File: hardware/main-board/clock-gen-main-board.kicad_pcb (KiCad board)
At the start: 2 copper layers, 70 x 50 mm, 18 parts, among them J1 Conn_01x03_Pin, J2 Conn_01x03_Pin, J3 Conn_01x02_Pin, J4 Conn_01x01_Pin, J5 Conn_01x01_Pin, J6 Conn_01x01_Pin, J7 Conn_01x01_Pin, U1 Pico

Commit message: fix iovdd
- create new gerbers
- create new render
- update readme
- update changelog
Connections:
- U1 pad 36: /PCM.3V3 -> /Gen.VSI
- U1 pad 39: /Gen.VSI -> unconnected-(U1-VSYS-Pad39)
- U3 pad 2: /PCM.3V3 -> /Gen.VSI
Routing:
- net /PCM.3V3: track 62.1 -> 0.00 mm
- net /Gen.VSI: track 50.9 -> 109.0 mm
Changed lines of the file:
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@@
   (title_block
     (title "${proj-title}")
-    (date "2023-09-16")
+    (date "2023-09-23")
     (rev "${proj-version}")
     (company "${proj-author}")
@@
   (property "proj-license" "CC BY-SA 4.0")
   (property "proj-title" "clock-gen adc main board")
-  (property "proj-version" "A")
+  (property "proj-version" "B")
   (net 0 "")
   (net 1 "unconnected-(U1-GPIO0-Pad1)")
@@
   (net 14 "unconnected-(U1-GPIO15-Pad20)")
   (net 15 "Net-(D1-K)")
-  (net 16 "/PCM.3V3")
+  (net 16 "unconnected-(U1-VSYS-Pad39)")
   (net 17 "/PCM.Data")
   (net 18 "/PCM.BitClk")
@@
       (net 33 "/PCM.5V") (pinfunction "+5V") (pintype "power_in"))
     (pad "2" thru_hole circle (at -7.62 -2 180) (size 2 2) (drill 1.25) (layers "*.Cu" "*.Mask")
-      (net 16 "/PCM.3V3") (pinfunction "+3.3V") (pintype "power_in"))
+      (net 38 "/Gen.VSI") (pinfunction "+3.3V") (pintype "power_in"))
     (pad "3" thru_hole circle (at -5.08 -2 180) (size 2 2) (drill 1.25) (layers "*.Cu" "*.Mask")
       (net 30 "GND") (pinfunction "GND") (pintype "power_in"))
@@
       (net 25 "unconnected-(U1-ADC_VREF-Pad35)") (pinfunction "ADC_VREF") (pintype "power_in+no_connect"))
     (pad "36" thru_hole oval (at 8.89 -13.97 90) (size 1.7 1.7) (drill 1.02) (layers "*.Cu" "*.Mask")
-      (net 16 "/PCM.3V3") (pinfunction "3V3") (pintype "power_in"))
+      (net 38 "/Gen.VSI") (pinfunction "3V3") (pintype "power_in"))
     (pad "36" smd rect (at 8.89 -13.97 90) (size 3.5 1.7) (drill (offset 0.9 0)) (layers "F.Cu" "F.Mask")
-      (net 16 "/PCM.3V3") (pinfunction "3V3") (pintype "power_in"))
+      (net 38 "/Gen.VSI") (pinfunction "3V3") (pintype "power_in"))
     (pad "37" thru_hole oval (at 8.89 -16.51 90) (size 1.7 1.7) (drill 1.02) (layers "*.Cu" "*.Mask")
       (net 26 "unconnected-(U1-3V3_EN-Pad37)") (pinfunction "3V3_EN") (pintype "input+no_connect"))
@@
       (net 30 "GND") (pinfunction "GND") (pintype "bidirectional"))
     (pad "39" thru_hole oval (at 8.89 -21.59 90) (size 1.7 1.7) (drill 1.02) (layers "*.Cu" "*.Mask")
-      (net 38 "/Gen.VSI") (pinfunction "VSYS") (pintype "power_in"))
+      (net 16 "unconnected-(U1-VSYS-Pad39)") (pinfunction "VSYS") (pintype "power_in+no_connect"))
     (pad "39" smd rect (at 8.89 -21.59 90) (size 3.5 1.7) (drill (offset 0.9 0)) (layers "F.Cu" "F.Mask")
-      (net 38 "/Gen.VSI") (pinfunction "VSYS") (pintype "power_in"))
+      (net 16 "unconnected-(U1-VSYS-Pad39)") (pinfunction "VSYS") (pintype "power_in+no_connect"))
     (pad "40" thru_hole oval (at 8.89 -24.13 90) (size 1.7 1.7) (drill 1.02) (layers "*.Cu" "*.Mask")
       (net 33 "/PCM.5V") (pinfunction "VBUS") (pintype "power_in"))
@@
   (segment (start 148.63 91.16) (end 148.63 87.83) (width 0.25) (layer "F.Cu") (net 15))
   (segment (start 148.63 87.83) (end 145.55 84.75) (width 0.25) (layer "F.Cu") (net 15))
-  (segment (start 152.2 105.6) (end 156.37 109.77) (width 0.25) (layer "F.Cu") (net 16))
-  (segment (start 156.37 109.77) (end 156.37 116.4345) (width 0.25) (layer "F.Cu") (net 16))
-  (segment (start 111 94.8) (end 119.2 94.8) (width 0.25) (layer "F.Cu") (net 16))
-  (segment (start 119.2 94.8) (end 130 105.6) (width 0.25) (layer "F.Cu") (net 16))
-  (segment (start 110.6 91.23) (end 110.6 94.4) (width 0.25) (layer "F.Cu") (net 16))
-  (segment (start 110.6 94.4) (end 111 94.8) (width 0.25) (layer "F.Cu") (net 16))
-  (segment (start 110.53 91.16) (end 110.6 91.23) (width 0.25) (layer "F.Cu") (net 16))
-  (segment (start 130 105.6) (end 152.2 105.6) (width 0.25) (layer "F.Cu") (net 16))
   (segment (start 150.4 104.6) (end 152 106.2) (width 0.25) (layer "B.Cu") (net 17))
   (segment (start 152 106.2) (end 152 114) (width 0.25) (layer "B.Cu") (net 17))
@@
   (segment (start 141.4 118.8) (end 141.13 118.53) (width 0.25) (layer "F.Cu") (net 37))
   (segment (start 160.2 118.8) (end 141.4 118.8) (width 0.25) (layer "F.Cu") (net 37))
-  (segment (start 102.91 92.91) (end 107.6 97.6) (width 0.25) (layer "F.Cu") (net 38))
   (segment (start 99 106.6) (end 99 114) (width 0.25) (layer "F.Cu") (net 38))
+  (segment (start 152.2 105.6) (end 156.37 109.77) (width 0.25) (layer "F.Cu") (net 38))
+  (segment (start 156.37 109.77) (end 156.37 116.4345) (width 0.25) (layer "F.Cu") (net 38))
   (segment (start 99 114) (end 99.4 114.4) (width 0.25) (layer "F.Cu") (net 38))
+  (segment (start 111 94.8) (end 119.2 94.8) (width 0.25) (layer "F.Cu") (net 38))
   (segment (start 101.6 114.4) (end 113.244 126.044) (width 0.25) (layer "F.Cu") (net 38))
   (segment (start 107.6 103.4) (end 104.8 106.2) (width 0.25) (layer "F.Cu") (net 38))
   (segment (start 113.244 126.044) (end 113.38 126.044) (width 0.25) (layer "F.Cu") (net 38))
+  (segment (start 119.2 94.8) (end 130 105.6) (width 0.25) (layer "F.Cu") (net 38))
+  (segment (start 110.6 91.23) (end 110.6 94.4) (width 0.25) (layer "F.Cu") (net 38))
   (segment (start 99.4 114.4) (end 101.6 114.4) (width 0.25) (layer "F.Cu") (net 38))
-  (segment (start 102.91 91.16) (end 102.91 92.91) (width 0.25) (layer "F.Cu") (net 38))
+  (segment (start 110.6 94.6) (end 110.6 94.4) (width 0.25) (layer "F.Cu") (net 38))
+  (segment (start 110.6 94.4) (end 111 94.8) (width 0.25) (layer "F.Cu") (net 38))
   (segment (start 99.4 106.2) (end 99 106.6) (width 0.25) (layer "F.Cu") (net 38))
+  (segment (start 110.53 91.16) (end 110.6 91.23) (width 0.25) (layer "F.Cu") (net 38))
   (segment (start 107.6 97.6) (end 107.6 103.4) (width 0.25) (layer "F.Cu") (net 38))
+  (segment (start 107.6 97.6) (end 110.6 94.6) (width 0.25) (layer "F.Cu") (net 38))
   (segment (start 104.8 106.2) (end 99.4 106.2) (width 0.25) (layer "F.Cu") (net 38))
+  (segment (start 130 105.6) (end 152.2 105.6) (width 0.25) (layer "F.Cu") (net 38))
   (segment (start 130.6 83.8) (end 126.25 83.8) (width 0.25) (layer "F.Cu") (net 40))
   (segment (start 135 83.8) (end 130.6 83.8) (width 0.25) (layer "F.Cu") (net 40))

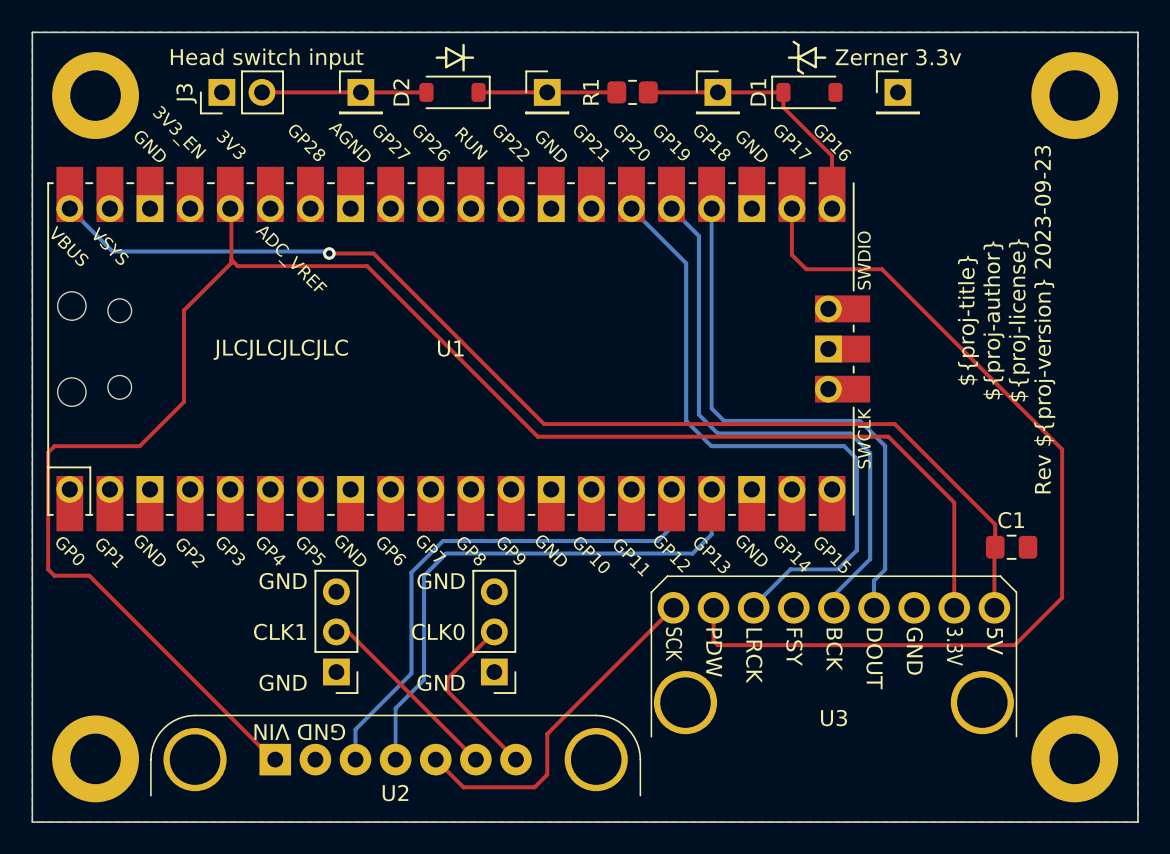
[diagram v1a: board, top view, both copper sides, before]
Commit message: Resolve "PCM1802 board 3.3V pin is driven instead of open"
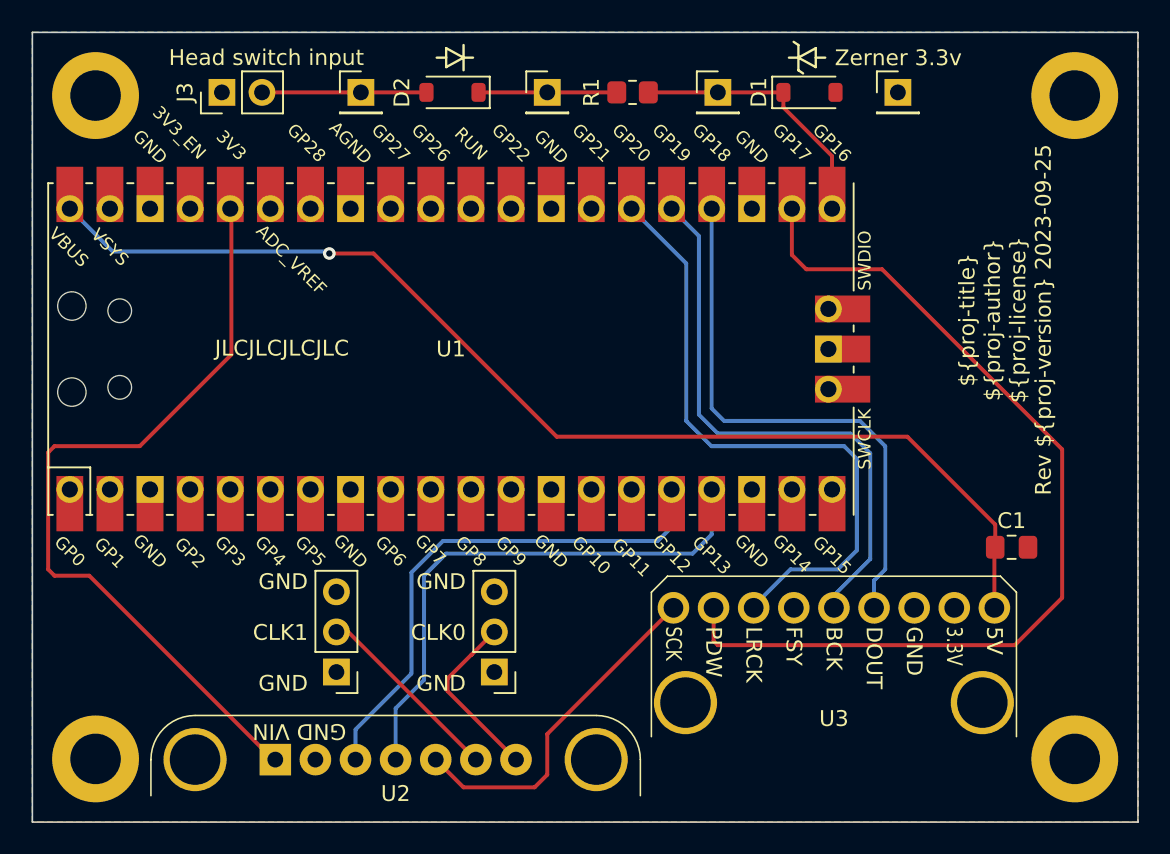
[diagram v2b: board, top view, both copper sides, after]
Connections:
- U3 pad 2: /Gen.VSI -> unconnected-(U3-+3.3V-Pad2)
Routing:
- net /Gen.VSI: track 109.0 -> 50.2 mm
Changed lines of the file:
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@@
   (title_block
     (title "${proj-title}")
-    (date "2023-09-23")
+    (date "2023-09-25")
     (rev "${proj-version}")
     (company "${proj-author}")
@@
   (property "proj-license" "CC BY-SA 4.0")
   (property "proj-title" "clock-gen adc main board")
-  (property "proj-version" "B")
+  (property "proj-version" "C")
   (net 0 "")
   (net 1 "unconnected-(U1-GPIO0-Pad1)")
@@
   (net 40 "Net-(D2-K)")
   (net 41 "Net-(D2-A)")
+  (net 42 "unconnected-(U3-+3.3V-Pad2)")
   (footprint "black-pcm1802:black-pcm1802-board" (layer "F.Cu")
     (at 148.75 114.4345 180)
@@
       (net 33 "/PCM.5V") (pinfunction "+5V") (pintype "power_in"))
     (pad "2" thru_hole circle (at -7.62 -2 180) (size 2 2) (drill 1.25) (layers "*.Cu" "*.Mask")
-      (net 38 "/Gen.VSI") (pinfunction "+3.3V") (pintype "power_in"))
+      (net 42 "unconnected-(U3-+3.3V-Pad2)") (pinfunction "+3.3V") (pintype "power_in+no_connect"))
     (pad "3" thru_hole circle (at -5.08 -2 180) (size 2 2) (drill 1.25) (layers "*.Cu" "*.Mask")
       (net 30 "GND") (pinfunction "GND") (pintype "power_in"))
@@
   (segment (start 126.08 126.044) (end 117.996 117.96) (width 0.25) (layer "F.Cu") (net 32))
   (segment (start 117.996 117.96) (end 117.25 117.96) (width 0.25) (layer "F.Cu") (net 32))
+  (segment (start 131.2 105.6) (end 119.6 94) (width 0.25) (layer "F.Cu") (net 33))
+  (segment (start 119.6 94) (end 116.8 94) (width 0.25) (layer "F.Cu") (net 33))
+  (segment (start 153.4 105.6) (end 131.2 105.6) (width 0.25) (layer "F.Cu") (net 33))
   (segment (start 159 112.6375) (end 158.91 112.7275) (width 0.25) (layer "F.Cu") (net 33))
-  (segment (start 152.6 104.8) (end 130.4 104.8) (width 0.25) (layer "F.Cu") (net 33))
   (segment (start 159 112.6375) (end 158.9625 112.6) (width 0.25) (layer "F.Cu") (net 33))
   (segment (start 158.91 112.7275) (end 158.91 116.4345) (width 0.25) (layer "F.Cu") (net 33))
   (segment (start 158.9625 112.6) (end 158.9625 111.1625) (width 0.25) (layer "F.Cu") (net 33))
-  (segment (start 158.9625 111.1625) (end 152.6 104.8) (width 0.25) (layer "F.Cu") (net 33))
-  (segment (start 119.6 94) (end 116.8 94) (width 0.25) (layer "F.Cu") (net 33))
-  (segment (start 130.4 104.8) (end 119.6 94) (width 0.25) (layer "F.Cu") (net 33))
+  (segment (start 158.9625 111.1625) (end 153.4 105.6) (width 0.25) (layer "F.Cu") (net 33))
   (via (at 116.8 94) (size 0.8) (drill 0.4) (layers "F.Cu" "B.Cu") (net 33))
   (segment (start 116.6755 93.8755) (end 103.0855 93.8755) (width 0.25) (layer "B.Cu") (net 33))
@@
   (segment (start 141.4 118.8) (end 141.13 118.53) (width 0.25) (layer "F.Cu") (net 37))
   (segment (start 160.2 118.8) (end 141.4 118.8) (width 0.25) (layer "F.Cu") (net 37))
+  (segment (start 99.4 114.4) (end 101.6 114.4) (width 0.25) (layer "F.Cu") (net 38))
+  (segment (start 104.8 106.2) (end 99.4 106.2) (width 0.25) (layer "F.Cu") (net 38))
   (segment (start 99 106.6) (end 99 114) (width 0.25) (layer "F.Cu") (net 38))
-  (segment (start 152.2 105.6) (end 156.37 109.77) (width 0.25) (layer "F.Cu") (net 38))
-  (segment (start 156.37 109.77) (end 156.37 116.4345) (width 0.25) (layer "F.Cu") (net 38))
+  (segment (start 99.4 106.2) (end 99 106.6) (width 0.25) (layer "F.Cu") (net 38))
+  (segment (start 101.6 114.4) (end 113.244 126.044) (width 0.25) (layer "F.Cu") (net 38))
+  (segment (start 110.6 91.23) (end 110.6 100.4) (width 0.25) (layer "F.Cu") (net 38))
+  (segment (start 110.53 91.16) (end 110.6 91.23) (width 0.25) (layer "F.Cu") (net 38))
+  (segment (start 110.6 100.4) (end 104.8 106.2) (width 0.25) (layer "F.Cu") (net 38))
+  (segment (start 113.244 126.044) (end 113.38 126.044) (width 0.25) (layer "F.Cu") (net 38))
   (segment (start 99 114) (end 99.4 114.4) (width 0.25) (layer "F.Cu") (net 38))
-  (segment (start 111 94.8) (end 119.2 94.8) (width 0.25) (layer "F.Cu") (net 38))
-  (segment (start 101.6 114.4) (end 113.244 126.044) (width 0.25) (layer "F.Cu") (net 38))
-  (segment (start 107.6 103.4) (end 104.8 106.2) (width 0.25) (layer "F.Cu") (net 38))
-  (segment (start 113.244 126.044) (end 113.38 126.044) (width 0.25) (layer "F.Cu") (net 38))
-  (segment (start 119.2 94.8) (end 130 105.6) (width 0.25) (layer "F.Cu") (net 38))
-  (segment (start 110.6 91.23) (end 110.6 94.4) (width 0.25) (layer "F.Cu") (net 38))
-  (segment (start 99.4 114.4) (end 101.6 114.4) (width 0.25) (layer "F.Cu") (net 38))
-  (segment (start 110.6 94.6) (end 110.6 94.4) (width 0.25) (layer "F.Cu") (net 38))
-  (segment (start 110.6 94.4) (end 111 94.8) (width 0.25) (layer "F.Cu") (net 38))
-  (segment (start 99.4 106.2) (end 99 106.6) (width 0.25) (layer "F.Cu") (net 38))
-  (segment (start 110.53 91.16) (end 110.6 91.23) (width 0.25) (layer "F.Cu") (net 38))
-  (segment (start 107.6 97.6) (end 107.6 103.4) (width 0.25) (layer "F.Cu") (net 38))
-  (segment (start 107.6 97.6) (end 110.6 94.6) (width 0.25) (layer "F.Cu") (net 38))
-  (segment (start 104.8 106.2) (end 99.4 106.2) (width 0.25) (layer "F.Cu") (net 38))
-  (segment (start 130 105.6) (end 152.2 105.6) (width 0.25) (layer "F.Cu") (net 38))
   (segment (start 130.6 83.8) (end 126.25 83.8) (width 0.25) (layer "F.Cu") (net 40))
   (segment (start 135 83.8) (end 130.6 83.8) (width 0.25) (layer "F.Cu") (net 40))

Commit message: Resolve "PCBway Compatible Gerbers"
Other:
- board text added: "${fab-jlc}"
- board text removed: "JLCJLCJLCJLC"
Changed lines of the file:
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@@
       (plot_on_all_layers_selection 0x0000000_00000000)
       (disableapertmacros false)
-      (usegerberextensions true)
+      (usegerberextensions false)
       (usegerberattributes false)
       (usegerberadvancedattributes false)
@@
     )
   )
+  (property "fab-jlc" "JLCJLCJLCJLC")
+  (property "fab-pcbway" "WayWayWay")
   (property "proj-author" "Rene Wolf")
   (property "proj-license" "CC BY-SA 4.0")
@@
     (effects (font (size 1 1) (thickness 0.15)) (justify right))
   )
-  (gr_text "JLCJLCJLCJLC" (at 113.8 100) (layer "F.SilkS")
+  (gr_text "${fab-jlc}" (at 113.8 100) (layer "F.SilkS")
     (effects (font (size 1 1) (thickness 0.15)))
   )
